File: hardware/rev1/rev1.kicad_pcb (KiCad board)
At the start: 2 copper layers, 65.2 x 53.6 mm, 28 parts, among them U1 BNO055, U2 MPL3115A2, U3 Teensy3.6, Y1 Crystal_32kHz768

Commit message: wip
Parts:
- added C10: C_0.1uF, footprints:C_0805_OEM, F.Cu at (106.3, 115.3)
- added C11: C_1uF, footprints:C_0805_OEM, F.Cu at (110.6, 115.3)
- added C12: C_100nF, footprints:C_0603_1608Metric, F.Cu at (178.5, 121.6)
- added C13: C_100nF, footprints:C_0603_1608Metric, F.Cu at (178.5, 125.7)
- added U4: BMI088, footprints:bmi088, F.Cu at (178.9, 116.1)
- added U5: ADXL345BCCZ, ADXL345_snapEda:ADXL345, F.Cu at (115.8, 113.3)
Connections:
- net Net-(U3-Pad30) renamed TX
- net Net-(U3-Pad31) renamed RX
- net Net-(U3-Pad32) renamed ENABLE_GPS
- net Net-(U3-Pad33) renamed PPS
- net Net-(U3-Pad35) renamed FIX
- U3 pad 18: Net-(U3-Pad18) -> A0_ACCEL_BMI088
- U3 pad 19: Net-(U3-Pad19) -> A0_GYRO_BMI088
- U3 pad 2: Net-(U3-Pad2) -> INT1_ADXL345
- U3 pad 21: Net-(U3-Pad21) -> INT4_GYRO_BMI088
- U3 pad 22: Net-(U3-Pad22) -> INT3_GYRO_BMI088
- U3 pad 23: Net-(U3-Pad23) -> INT2_ACCEL_BMI088
- U3 pad 24: Net-(U3-Pad24) -> INT1_ACCEL_BMI088
- U3 pad 3: Net-(U3-Pad3) -> INT2_ADXL345
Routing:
- removed copper zone on B.Cu, net GND
- removed copper zone on F.Cu, net GND
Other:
- board outline removed

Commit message: wip
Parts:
- moved C13 6.93 mm to (178.8, 118.7)
- moved C12 6.17 mm to (178.8, 115.4)
- moved U4 5.09 mm to (179.1, 111.1)
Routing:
- net VDD: track 182.7 -> 252.9 mm
- net GND: track 84.1 -> 133.7 mm, vias 8 -> 16
- net SDA_TEENSY: track 45.3 -> 87.3 mm, vias 2 -> 5
- net SCL_TEENSY: track 50.5 -> 89.4 mm, vias 2 -> 4
- net INT1_ADXL345: track 0.00 -> 15.5 mm, vias 0 -> 2
- net INT2_ADXL345: track 0.00 -> 15.1 mm, vias 0 -> 2
- net INT_BNO055: track 30.8 -> 31.6 mm

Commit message: wip
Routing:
- net VDD: track 252.9 -> 275.7 mm
- net A0_GYRO_BMI088: track 0.00 -> 13.5 mm
- net GND: track 133.7 -> 138.7 mm, vias 16 -> 18
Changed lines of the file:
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@@
     (thickness 1.6)
     (drawings 0)
-    (tracks 437)
+    (tracks 457)
     (zones 0)
     (modules 34)
@@
   )
   (setup
-    (last_trace_width 1)
+    (last_trace_width 0.25)
     (user_trace_width 1)
     (trace_clearance 0.2)
@@
   (segment (start 114.814 113.684) (end 114.814 114.046) (width 0.25) (layer F.Cu) (net 1) (status 400000))
   (segment (start 114.814 114.046) (end 114.814 114.484) (width 0.25) (layer F.Cu) (net 1) (status 800000))
-  (segment (start 106.299 114.316) (end 110.617 114.316) (width 1) (layer F.Cu) (net 1) (status C00000))
+  (segment (start 106.299 114.316) (end 108.458 114.316) (width 1) (layer F.Cu) (net 1) (status 400000))
+  (segment (start 108.458 114.316) (end 110.617 114.316) (width 1) (layer F.Cu) (net 1) (status 800000))
   (segment (start 110.617 114.316) (end 113.776 114.316) (width 1) (layer F.Cu) (net 1) (status 400000))
   (segment (start 113.776 114.316) (end 113.792 114.3) (width 1) (layer F.Cu) (net 1))
@@
   (segment (start 179.1335 112.3215) (end 179.1335 113.0935) (width 0.25) (layer F.Cu) (net 1) (status 400000))
   (segment (start 179.1335 113.0935) (end 178.054 114.173) (width 0.25) (layer F.Cu) (net 1))
+  (segment (start 108.458 114.316) (end 108.458 112.903) (width 1) (layer F.Cu) (net 1))
+  (via (at 108.458 109.347) (size 1.2) (drill 0.6) (layers F.Cu B.Cu) (net 1))
+  (via (at 108.458 112.903) (size 1.2) (drill 0.6) (layers F.Cu B.Cu) (net 1))
+  (segment (start 108.458 112.903) (end 108.458 109.347) (width 1) (layer B.Cu) (net 1))
   (segment (start 146.8595 126.6825) (end 149.4155 124.1265) (width 1) (layer F.Cu) (net 2) (status 400000))
   (segment (start 149.098 124.444) (end 149.4155 124.1265) (width 1) (layer F.Cu) (net 2))
@@
   (segment (start 179.6035 115.443) (end 179.6035 114.4525) (width 1) (layer F.Cu) (net 2) (status 400000))
   (segment (start 179.6035 118.745) (end 179.6035 115.443) (width 1) (layer F.Cu) (net 2) (status C00000))
-  (segment (start 161.036 119.1235) (end 165.7325 119.1235) (width 1) (layer F.Cu) (net 2))
+  (segment (start 161.036 119.1235) (end 165.608 119.1235) (width 1) (layer F.Cu) (net 2))
+  (segment (start 165.608 119.1235) (end 165.7325 119.1235) (width 1) (layer F.Cu) (net 2))
   (segment (start 179.6035 119.8625) (end 179.6035 118.745) (width 1) (layer F.Cu) (net 2) (status 800000))
   (segment (start 178.816 120.65) (end 179.6035 119.8625) (width 1) (layer F.Cu) (net 2))
@@
   (segment (start 156.083 116.84) (end 157.099 116.84) (width 1) (layer F.Cu) (net 2))
   (segment (start 157.099 116.84) (end 157.226 116.967) (width 1) (layer F.Cu) (net 2))
+  (segment (start 163.2585 116.9035) (end 165.735 114.427) (width 1) (layer F.Cu) (net 2) (status 400000))
+  (segment (start 165.735 114.427) (end 166.751 113.411) (width 1) (layer F.Cu) (net 2))
+  (segment (start 177.308498 112.3215) (end 177.308498 112.268) (width 1) (layer F.Cu) (net 2))
+  (segment (start 177.254998 112.268) (end 177.308498 112.3215) (width 1) (layer F.Cu) (net 2))
+  (segment (start 177.165 112.268) (end 177.254998 112.268) (width 1) (layer F.Cu) (net 2))
+  (segment (start 166.751 113.411) (end 167.894 112.268) (width 1) (layer F.Cu) (net 2))
+  (segment (start 167.894 112.268) (end 177.308498 112.268) (width 1) (layer F.Cu) (net 2))
+  (segment (start 177.308498 112.268) (end 177.165 112.268) (width 1) (layer F.Cu) (net 2))
+  (segment (start 177.6335 112.3215) (end 177.308498 112.3215) (width 0.25) (layer F.Cu) (net 2) (status 400000))
+  (segment (start 165.608 119.1235) (end 165.608 114.554) (width 1) (layer F.Cu) (net 2))
+  (segment (start 165.608 114.554) (end 166.751 113.411) (width 1) (layer F.Cu) (net 2))
   (segment (start 153.7924 122.3109) (end 155.8389 122.3109) (width 0.25) (layer F.Cu) (net 3) (status 400000))
   (segment (start 155.8389 122.3109) (end 157.6785 124.1505) (width 0.25) (layer F.Cu) (net 3))
@@
   (segment (start 153.7924 119.8109) (end 154.305 119.8109) (width 0.25) (layer F.Cu) (net 14) (status 400000))
   (segment (start 154.305 119.8109) (end 154.3549 119.8109) (width 0.25) (layer F.Cu) (net 14))
+  (segment (start 178.1335 109.8015) (end 178.1335 109.2995) (width 0.25) (layer F.Cu) (net 59) (status 400000))
+  (segment (start 175.387 106.553) (end 166.243 106.553) (width 0.25) (layer F.Cu) (net 59))
+  (segment (start 178.1335 109.2995) (end 175.387 106.553) (width 0.25) (layer F.Cu) (net 59))
   (segment (start 116.834 114.484) (end 118.18 114.484) (width 0.25) (layer F.Cu) (net 69) (status 400000))
   (segment (start 120.523 106.045) (end 120.523 102.616) (width 0.25) (layer F.Cu) (net 69) (status 800000))

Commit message: wip
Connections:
- U3 pad 18: A0_ACCEL_BMI088 -> A0_GYRO_BMI088
- U3 pad 19: A0_GYRO_BMI088 -> A0_ACCEL_BMI088
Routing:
- net A0_ACCEL_BMI088: track 0.00 -> 25.1 mm
- net A0_GYRO_BMI088: track 13.5 -> 22.8 mm
- net INT4_GYRO_BMI088: track 0.00 -> 6.74 mm, vias 0 -> 1
- net VDD: track 275.7 -> 282.2 mm, vias 7 -> 9
- net INT3_GYRO_BMI088: track 0.00 -> 4.63 mm, vias 0 -> 1
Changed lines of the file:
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@@
     (thickness 1.6)
     (drawings 0)
-    (tracks 457)
+    (tracks 478)
     (zones 0)
     (modules 34)
@@
       (net 54 "Net-(U3-Pad17)"))
     (pad 18 thru_hole circle (at 13.97 7.62) (size 1.6 1.6) (drill 1.1) (layers *.Cu *.Mask)
+      (net 59 A0_GYRO_BMI088))
+    (pad 19 thru_hole circle (at 16.51 7.62) (size 1.6 1.6) (drill 1.1) (layers *.Cu *.Mask)
       (net 58 A0_ACCEL_BMI088))
-    (pad 19 thru_hole circle (at 16.51 7.62) (size 1.6 1.6) (drill 1.1) (layers *.Cu *.Mask)
-      (net 59 A0_GYRO_BMI088))
     (pad 20 thru_hole circle (at 19.05 7.62) (size 1.6 1.6) (drill 1.1) (layers *.Cu *.Mask)
       (net 24 "Net-(U3-Pad20)"))
@@
   (segment (start 165.608 119.1235) (end 165.608 114.554) (width 1) (layer F.Cu) (net 2))
   (segment (start 165.608 114.554) (end 166.751 113.411) (width 1) (layer F.Cu) (net 2))
+  (segment (start 178.6335 109.8015) (end 178.6335 108.2755) (width 0.25) (layer F.Cu) (net 2) (status 400000))
+  (via (at 178.181 107.823) (size 1.2) (drill 0.6) (layers F.Cu B.Cu) (net 2))
+  (segment (start 178.6335 108.2755) (end 178.181 107.823) (width 0.25) (layer F.Cu) (net 2))
+  (segment (start 180.1335 109.8015) (end 180.1335 106.0925) (width 0.25) (layer F.Cu) (net 2) (status 400000))
+  (via (at 179.705 105.664) (size 1.2) (drill 0.6) (layers F.Cu B.Cu) (net 2))
+  (segment (start 180.1335 106.0925) (end 179.705 105.664) (width 0.25) (layer F.Cu) (net 2))
   (segment (start 153.7924 122.3109) (end 155.8389 122.3109) (width 0.25) (layer F.Cu) (net 3) (status 400000))
   (segment (start 155.8389 122.3109) (end 157.6785 124.1505) (width 0.25) (layer F.Cu) (net 3))
@@
   (segment (start 115.824 110.744) (end 116.84 109.728) (width 0.25) (layer F.Cu) (net 10))
   (segment (start 177.1185 111.0615) (end 174.1805 111.0615) (width 0.25) (layer F.Cu) (net 10) (status 400000))
-  (via (at 161.417 108.585) (size 0.8) (drill 0.4) (layers F.Cu B.Cu) (net 10))
-  (segment (start 171.704 108.585) (end 161.417 108.585) (width 0.25) (layer F.Cu) (net 10))
-  (segment (start 174.1805 111.0615) (end 171.704 108.585) (width 0.25) (layer F.Cu) (net 10))
-  (segment (start 161.417 108.585) (end 153.162 108.585) (width 0.25) (layer B.Cu) (net 10))
+  (segment (start 169.545 108.585) (end 160.02 108.585) (width 0.25) (layer F.Cu) (net 10))
+  (segment (start 172.0215 111.0615) (end 169.545 108.585) (width 0.25) (layer F.Cu) (net 10))
+  (segment (start 174.1805 111.0615) (end 172.0215 111.0615) (width 0.25) (layer F.Cu) (net 10))
+  (segment (start 153.162 108.585) (end 149.098 108.585) (width 0.25) (layer F.Cu) (net 10))
   (via (at 153.162 108.585) (size 0.8) (drill 0.4) (layers F.Cu B.Cu) (net 10))
-  (segment (start 153.162 108.585) (end 149.098 108.585) (width 0.25) (layer F.Cu) (net 10))
+  (segment (start 160.02 108.585) (end 153.162 108.585) (width 0.25) (layer B.Cu) (net 10))
+  (via (at 160.02 108.585) (size 0.8) (drill 0.4) (layers F.Cu B.Cu) (net 10))
   (segment (start 126.8049 116.3119) (end 126.8049 113.8601) (width 0.25) (layer F.Cu) (net 11) (status 400000))
   (segment (start 133.223 107.442) (end 133.223 104.267) (width 0.25) (layer F.Cu) (net 11))
@@
   (segment (start 153.7924 119.8109) (end 154.305 119.8109) (width 0.25) (layer F.Cu) (net 14) (status 400000))
   (segment (start 154.305 119.8109) (end 154.3549 119.8109) (width 0.25) (layer F.Cu) (net 14))
+  (segment (start 161.163 102.616) (end 163.195 104.648) (width 0.25) (layer F.Cu) (net 58) (status 400000))
+  (segment (start 180.6335 105.1955) (end 180.6335 109.8015) (width 0.25) (layer F.Cu) (net 58) (status 800000))
+  (segment (start 180.086 104.648) (end 180.6335 105.1955) (width 0.25) (layer F.Cu) (net 58))
+  (segment (start 178.816 104.648) (end 180.086 104.648) (width 0.25) (layer F.Cu) (net 58))
+  (segment (start 178.816 104.648) (end 163.195 104.648) (width 0.25) (layer F.Cu) (net 58))
   (segment (start 178.1335 109.8015) (end 178.1335 109.2995) (width 0.25) (layer F.Cu) (net 59) (status 400000))
-  (segment (start 175.387 106.553) (end 166.243 106.553) (width 0.25) (layer F.Cu) (net 59))
-  (segment (start 178.1335 109.2995) (end 175.387 106.553) (width 0.25) (layer F.Cu) (net 59))
+  (segment (start 163.195 107.188) (end 158.623 102.616) (width 0.25) (layer F.Cu) (net 59) (status 800000))
+  (segment (start 178.1335 109.2995) (end 176.022 107.188) (width 0.25) (layer F.Cu) (net 59))
+  (segment (start 176.022 107.188) (end 163.195 107.188) (width 0.25) (layer F.Cu) (net 59))
+  (segment (start 179.6335 109.8015) (end 179.6335 106.9895) (width 0.25) (layer F.Cu) (net 60) (status 400000))
+  (via (at 176.149 105.918) (size 0.8) (drill 0.4) (layers F.Cu B.Cu) (net 60))
+  (segment (start 178.562 105.918) (end 176.149 105.918) (width 0.25) (layer F.Cu) (net 60))
+  (segment (start 179.6335 106.9895) (end 178.562 105.918) (width 0.25) (layer F.Cu) (net 60))
+  (segment (start 179.1335 109.8015) (end 179.1335 107.2515) (width 0.25) (layer F.Cu) (net 61) (status 400000))
+  (via (at 177.292 106.68) (size 0.8) (drill 0.4) (layers F.Cu B.Cu) (net 61))
+  (segment (start 178.562 106.68) (end 177.292 106.68) (width 0.25) (layer F.Cu) (net 61))
+  (segment (start 179.1335 107.2515) (end 178.562 106.68) (width 0.25) (layer F.Cu) (net 61))
   (segment (start 116.834 114.484) (end 118.18 114.484) (width 0.25) (layer F.Cu) (net 69) (status 400000))
   (segment (start 120.523 106.045) (end 120.523 102.616) (width 0.25) (layer F.Cu) (net 69) (status 800000))

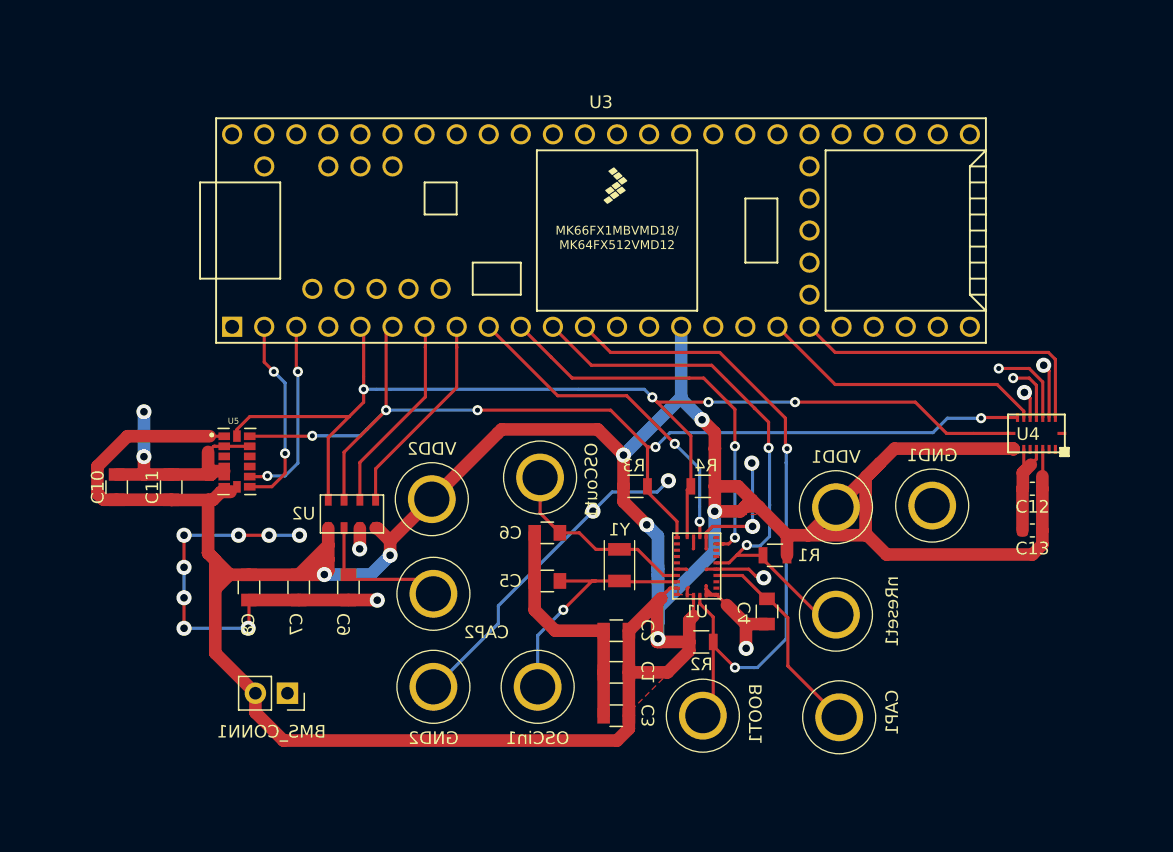
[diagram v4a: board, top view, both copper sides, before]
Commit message: add ADXL345 and BMI088 to layout
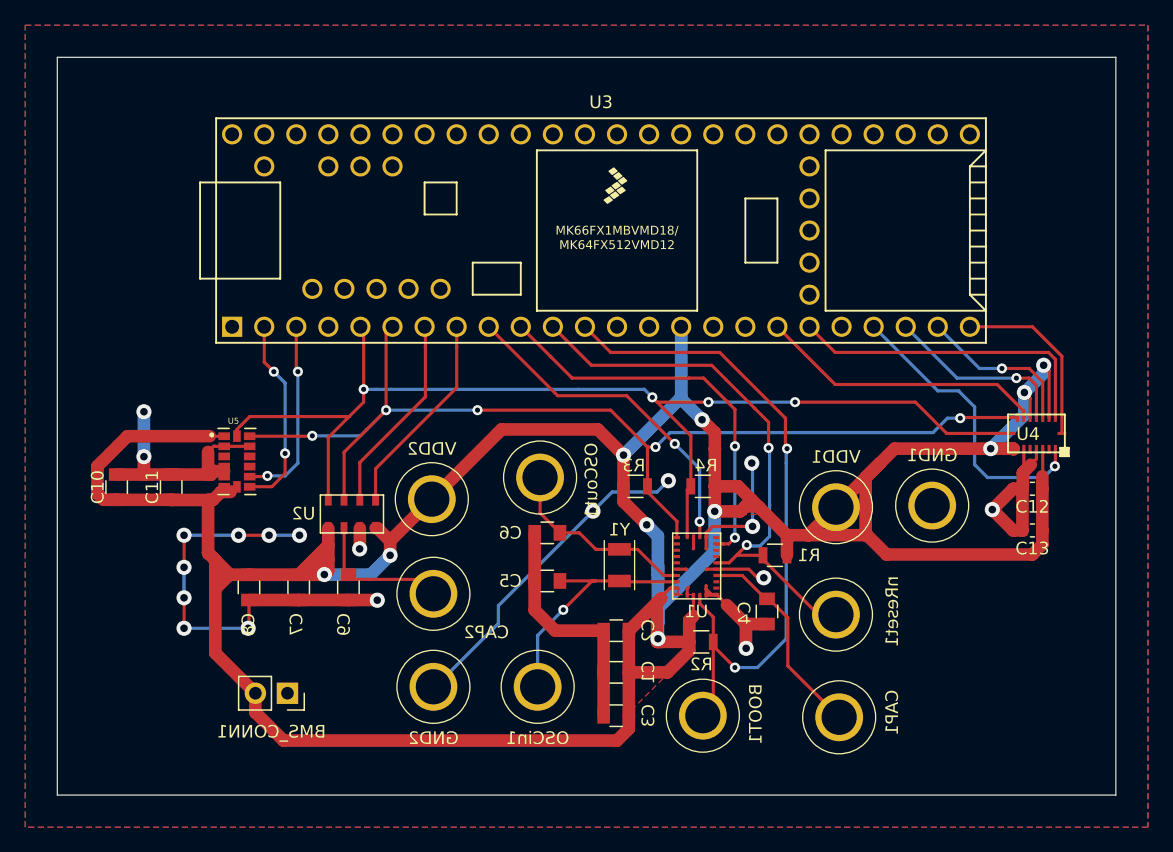
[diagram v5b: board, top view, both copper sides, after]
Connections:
- U3 pad 21: INT4_GYRO_BMI088 -> INT2_ACCEL_BMI088
- U3 pad 23: INT2_ACCEL_BMI088 -> INT4_GYRO_BMI088
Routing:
- net INT2_ACCEL_BMI088: track 0.00 -> 23.7 mm, vias 0 -> 1
- net INT1_ACCEL_BMI088: track 0.00 -> 14.4 mm
- net INT3_GYRO_BMI088: track 4.63 -> 14.8 mm
- net VDD: track 282.2 -> 290.6 mm, vias 9 -> 10
- net INT4_GYRO_BMI088: track 6.74 -> 12.9 mm
- net GND: track 138.7 -> 144.8 mm, vias 18 -> 19
- added copper zone on B.Cu, net GND
- added copper zone on F.Cu, net GND
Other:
- board outline added: 83.8 x 58.4 mm

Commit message: touch up zones
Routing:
- net GND: track 144.8 -> 170.7 mm, vias 19 -> 22
- net SCL_TEENSY: track 89.4 -> 90.1 mm
